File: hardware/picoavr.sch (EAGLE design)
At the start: 25 parts, among them IC1 MCP1703CB, Q2 12mhz, SW1 SPST_TACT-KMR2, U3 ATMEGA328P, X1 Micro USB

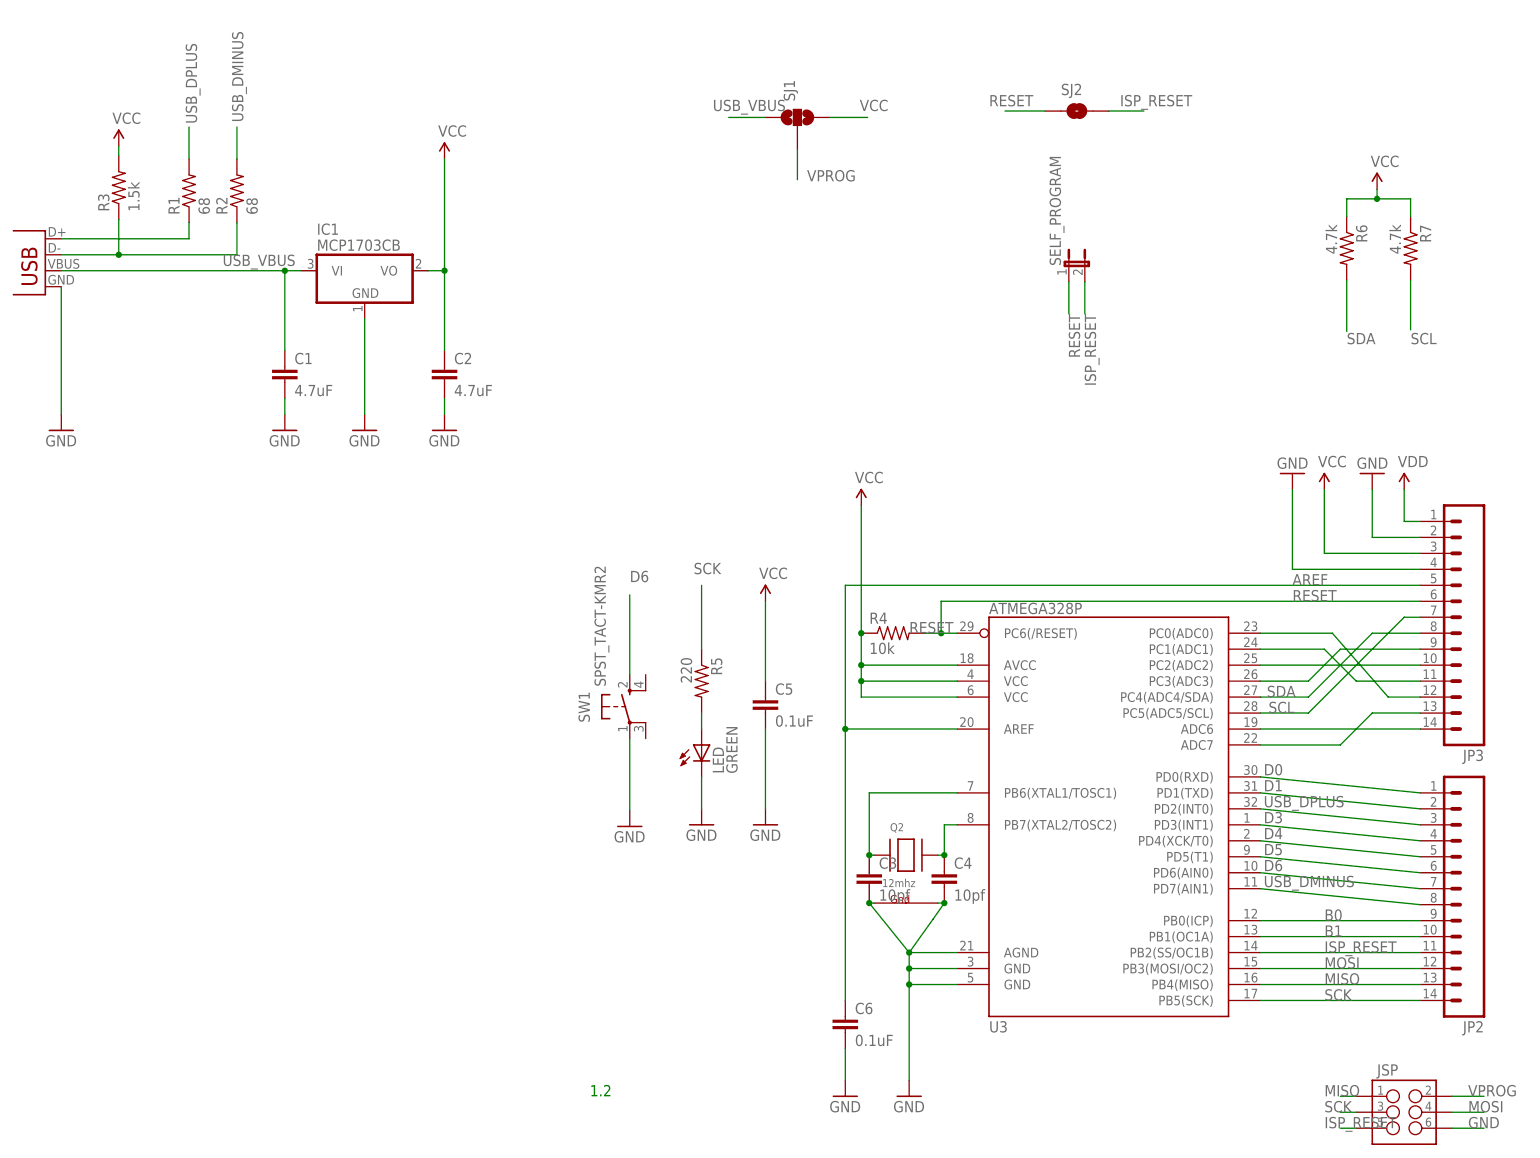
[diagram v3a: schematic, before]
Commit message: add optional reset button
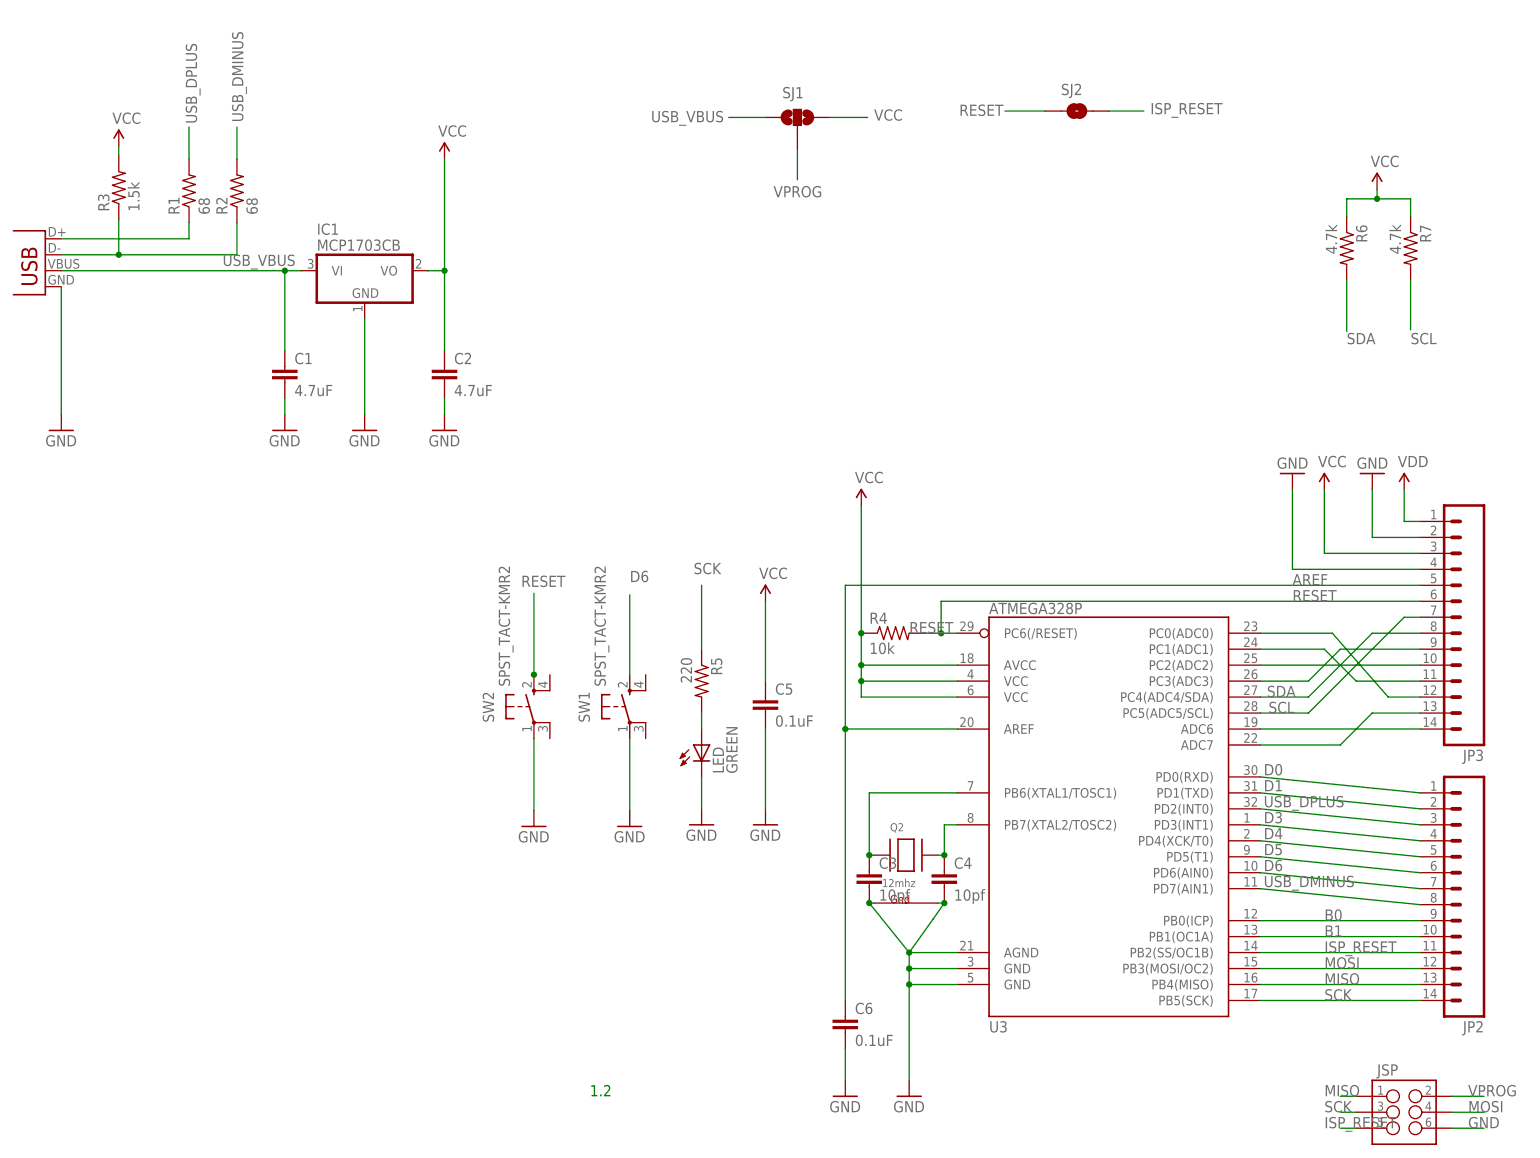
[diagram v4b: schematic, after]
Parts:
- removed SELF_PROGRAM: (no value), SparkFun-Passives:JUMPER-2PTH
- added SW2: SPST_TACT-KMR2, adafruit:SPST_TACT-KMR2
- SJ1: value (none) -> SJ1
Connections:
- net GND: now also SW2.P
- net ISP_RESET: no longer SELF_PROGRAM.2
- net RESET: now also SW2.S; no longer SELF_PROGRAM.1
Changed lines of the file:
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@@
 <part name="C4" library="SparkFun-Capacitors" deviceset="CAP" device="0402-CAP" value="10pf"/>
 <part name="Q2" library="adafruit" deviceset="XTAL-4" device="-3225" value="12mhz"/>
-<part name="SELF_PROGRAM" library="SparkFun-Passives" deviceset="JUMPER-2" device="PTH"/>
 <part name="GND1" library="supply1" deviceset="GND" device=""/>
 <part name="VCC5" library="SparkFun-Aesthetics" deviceset="VCC" device=""/>
 <part name="R6" library="SparkFun" deviceset="RESISTOR" device="0402-RES" value="4.7k"/>
 <part name="R7" library="SparkFun" deviceset="RESISTOR" device="0402-RES" value="4.7k"/>
-<part name="SJ1" library="SparkFun-Passives" deviceset="SOLDERJUMPER_2WAY" device="S"/>
+<part name="SJ1" library="SparkFun-Passives" deviceset="SOLDERJUMPER_2WAY" device="S" value="SJ1"/>
 <part name="SJ2" library="SparkFun-Passives" deviceset="SOLDERJUMPER" device="NO"/>
 <part name="SW1" library="adafruit" deviceset="SPST_TACT" device="-KMR2"/>
+<part name="SW2" library="adafruit" deviceset="SPST_TACT" device="-KMR2"/>
+<part name="GND4" library="supply1" deviceset="GND" device=""/>
 </parts>
 <sheets>
@@
 <instance part="C4" gate="G$1" x="155.448" y="45.974"/>
 <instance part="Q2" gate="G$1" x="149.352" y="51.054"/>
-<instance part="SELF_PROGRAM" gate="A" x="175.26" y="144.78"/>
 <instance part="GND1" gate="1" x="105.41" y="55.626"/>
 <instance part="VCC5" gate="G$1" x="224.282" y="156.972"/>
 <instance part="R6" gate="G$1" x="219.456" y="147.574" rot="R270"/>
 <instance part="R7" gate="G$1" x="229.616" y="147.574" rot="R270"/>
-<instance part="SJ1" gate="G$1" x="132.08" y="168.402" rot="R90"/>
+<instance part="SJ1" gate="G$1" x="132.08" y="168.402" smashed="yes" rot="R90">
+<attribute name="NAME" x="129.667" y="171.45" size="1.778" layer="95"/>
+</instance>
 <instance part="SJ2" gate="1" x="176.53" y="169.418" smashed="yes">
 <attribute name="NAME" x="173.99" y="171.958" size="1.778" layer="95"/>
 </instance>
 <instance part="SW1" gate="G$1" x="105.41" y="74.676"/>
+<instance part="SW2" gate="G$1" x="90.17" y="74.676"/>
+<instance part="GND4" gate="1" x="90.17" y="55.626"/>
 </instances>
 <busses>
@@
 <pinref part="SW1" gate="G$1" pin="P"/>
 </segment>
+<segment>
+<pinref part="GND4" gate="1" pin="GND"/>
+<pinref part="SW2" gate="G$1" pin="P"/>
+<wire x1="90.17" y1="58.166" x2="90.17" y2="69.596" width="0.1524" layer="91"/>
+</segment>
 </net>
 <net name="VCC" class="0">
@@
 <pinref part="SJ1" gate="G$1" pin="3"/>
 <wire x1="137.16" y1="168.402" x2="143.256" y2="168.402" width="0.1524" layer="91"/>
-<label x="141.986" y="169.418" size="1.778" layer="95"/>
+<label x="144.272" y="167.894" size="1.778" layer="95"/>
 </segment>
 </net>
@@
 </segment>
 <segment>
-<pinref part="SELF_PROGRAM" gate="A" pin="1"/>
-<wire x1="175.26" y1="142.24" x2="175.26" y2="137.16" width="0.1524" layer="91"/>
-<label x="175.26" y="137.16" size="1.778" layer="95" rot="R270"/>
-</segment>
-<segment>
 <wire x1="171.45" y1="169.418" x2="165.1" y2="169.418" width="0.1524" layer="91"/>
 <pinref part="SJ2" gate="1" pin="1"/>
-<label x="162.56" y="170.18" size="1.778" layer="95"/>
+<label x="164.846" y="170.434" size="1.778" layer="95" rot="R180"/>
+</segment>
+<segment>
+<wire x1="90.17" y1="79.502" x2="90.17" y2="79.756" width="0.1524" layer="91"/>
+<label x="88.138" y="93.726" size="1.778" layer="95"/>
+<pinref part="SW2" gate="G$1" pin="S"/>
+<wire x1="90.17" y1="79.756" x2="90.17" y2="92.71" width="0.1524" layer="91"/>
+<junction x="90.17" y="79.756"/>
 </segment>
 </net>
@@
 </segment>
 <segment>
-<pinref part="SELF_PROGRAM" gate="A" pin="2"/>
-<wire x1="177.8" y1="142.24" x2="177.8" y2="137.16" width="0.1524" layer="91"/>
-<label x="177.8" y="137.16" size="1.778" layer="95" rot="R270"/>
-</segment>
-<segment>
 <pinref part="SJ2" gate="1" pin="2"/>
 <wire x1="181.61" y1="169.418" x2="187.198" y2="169.418" width="0.1524" layer="91"/>
-<label x="183.388" y="170.18" size="1.778" layer="95"/>
+<label x="188.214" y="168.91" size="1.778" layer="95"/>
 </segment>
 </net>
@@
 <pinref part="SJ1" gate="G$1" pin="1"/>
 <wire x1="127" y1="168.402" x2="121.158" y2="168.402" width="0.1524" layer="91"/>
-<label x="118.618" y="169.418" size="1.778" layer="95"/>
+<label x="120.396" y="169.418" size="1.778" layer="95" rot="R180"/>
 </segment>
 </net>
@@
 <pinref part="SJ1" gate="G$1" pin="2"/>
 <wire x1="132.08" y1="163.322" x2="132.08" y2="158.496" width="0.1524" layer="91"/>
-<label x="133.604" y="158.242" size="1.778" layer="95"/>
-</segment>
-</net>
+<label x="128.27" y="155.702" size="1.778" layer="95"/>
+</segment>
+</net>
